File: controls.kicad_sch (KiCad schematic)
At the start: 29 parts, among them J10 IN 1x6h, J11 SYNC, J12 PWM, J13 CV, J14 1VOct, J15 FM, J19 CV 1x6h, J2 SQR, J21 LED 1x2h, J22 OCT 1x6h, J3 OUT 1x4h, J4 SAW, J5 TRI, J6 SIN, J7 CTRL 1x8h, SW1 SW_SPDT, U5 RS1702A0A-HA1

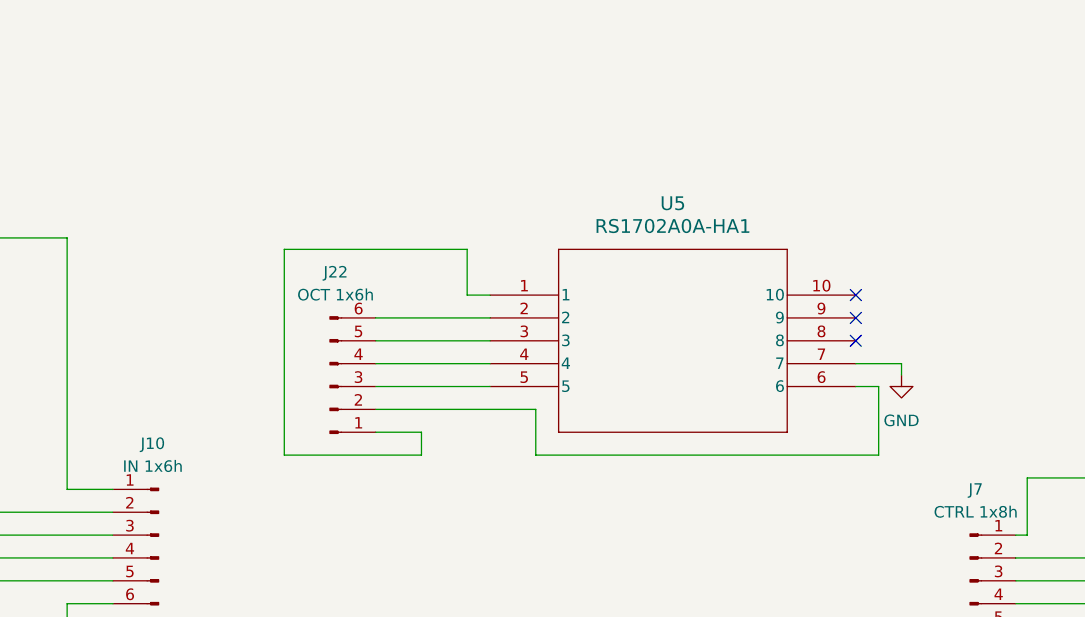
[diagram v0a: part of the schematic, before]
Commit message: Fixed oct selector and updated gnd islands on main
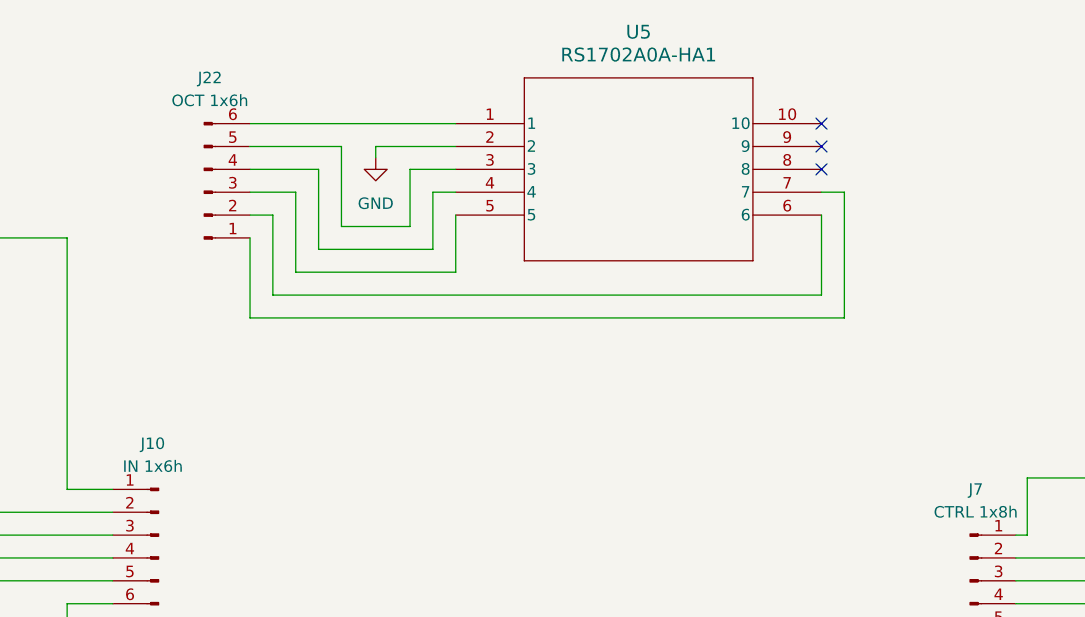
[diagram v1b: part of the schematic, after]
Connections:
- net GND: now also U5.2; no longer U5.7
- net at J22.1 (Pin_1): now also U5.7; no longer U5.1
- net at J22.6 (Pin_6): now also U5.1; no longer U5.2
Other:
- moved on the sheet: J22, U5
